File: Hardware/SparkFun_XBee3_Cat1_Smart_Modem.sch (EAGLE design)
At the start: 71 parts, among them J1 USB Female Type C Connector, J3 USB Female Type C Connector, J4 QWIIC_RIGHT_ANGLE, Q2 3.1A/30V/105mΩ, U1 FSUSB30MUX_MSOP10, U2 AP63203, U3 ESD Diode, U5 ESD Diode, U7 FT231XS

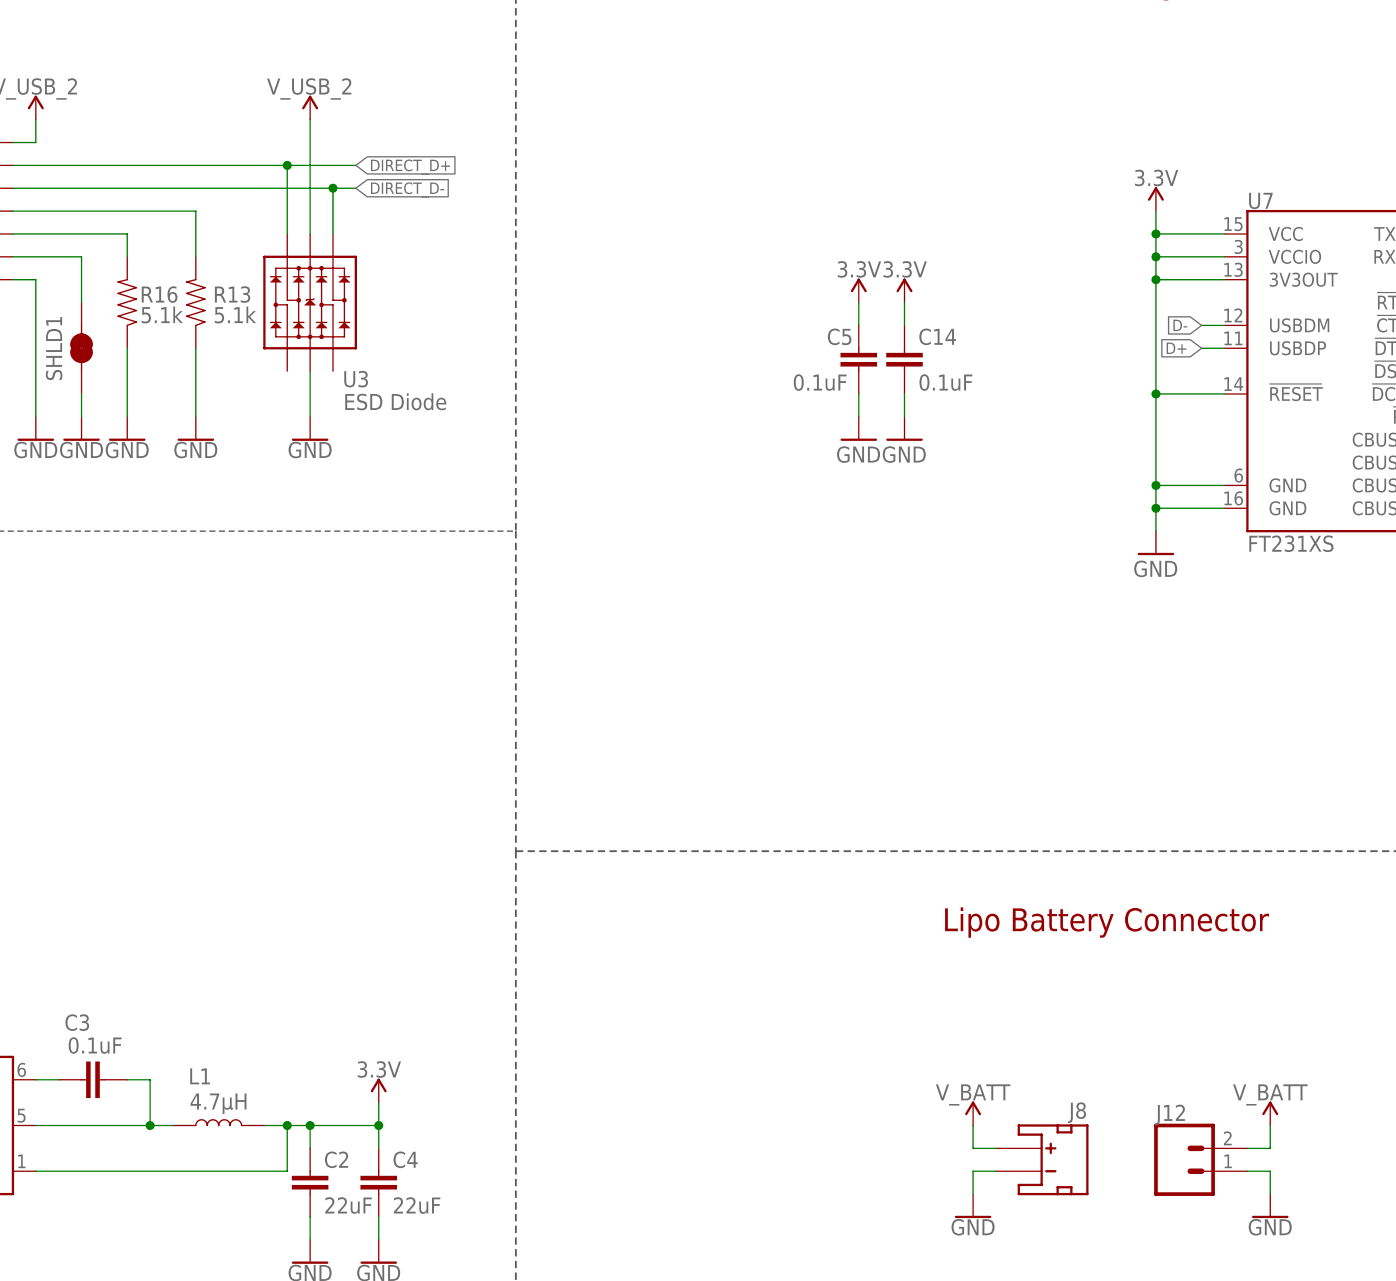
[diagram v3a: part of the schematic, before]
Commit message: Adds new 3.9uH Inductor
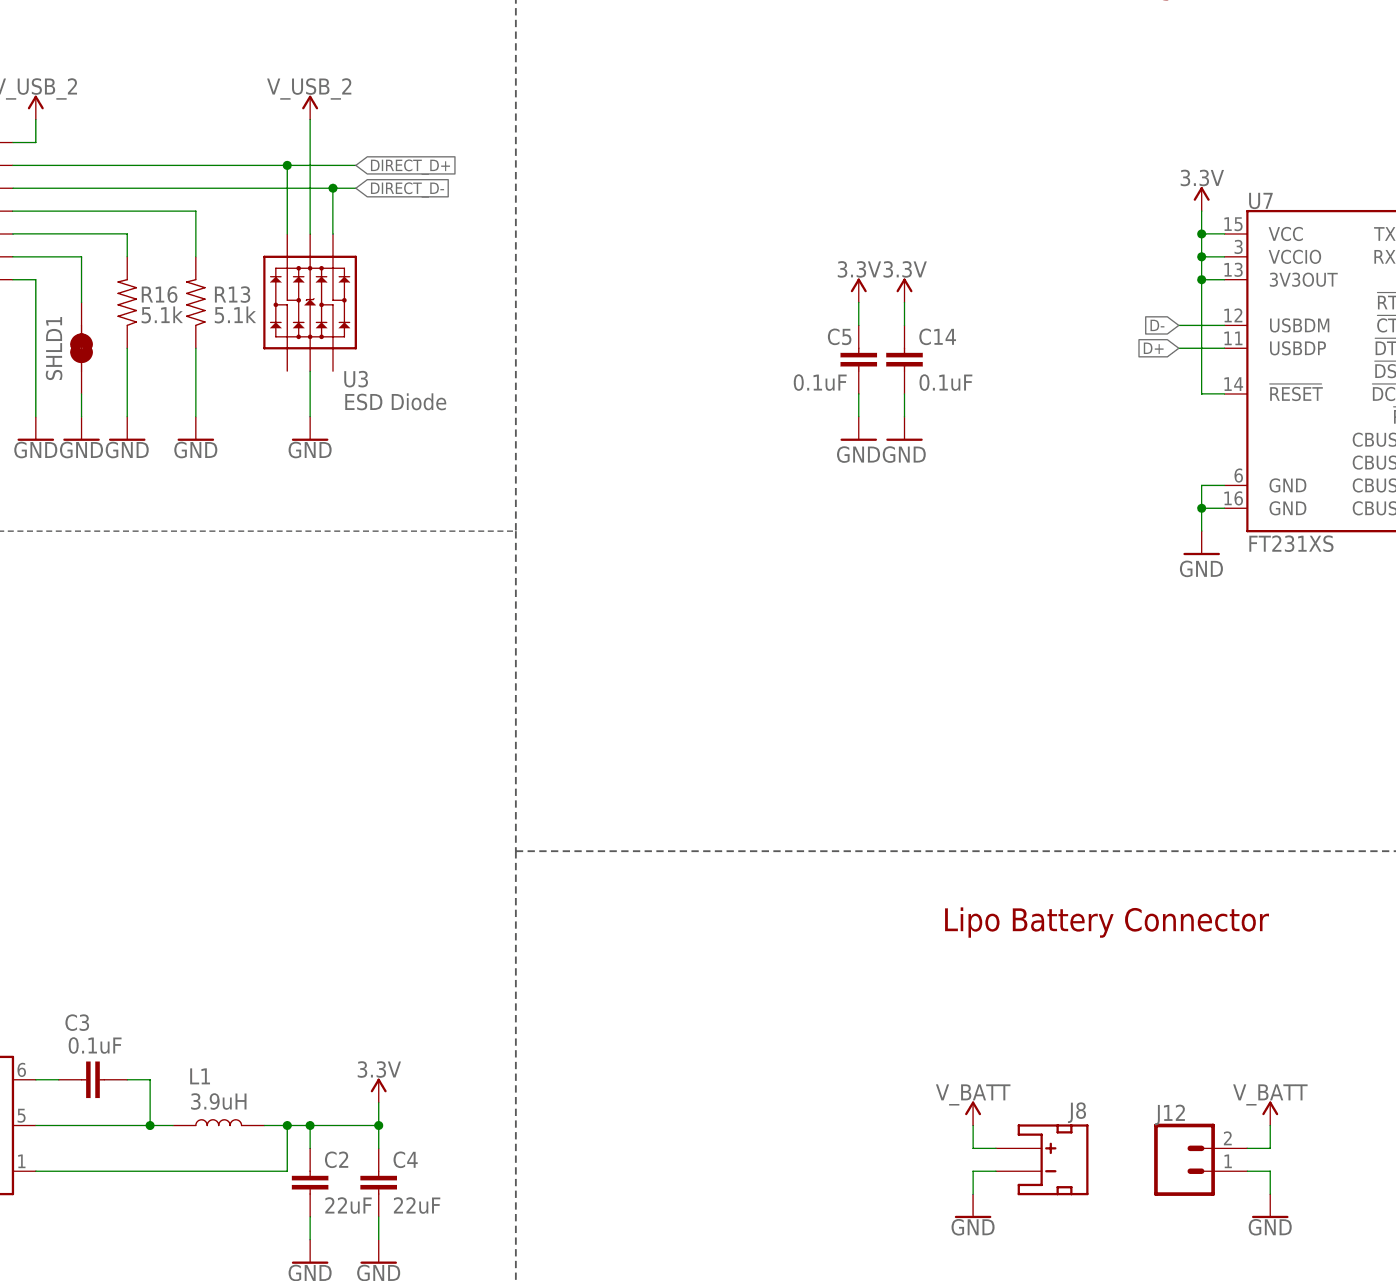
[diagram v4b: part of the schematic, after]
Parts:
- L1: value 4.7μH -> 3.9uH; device SparkFun-Coils:4.7μH_SHIELDED_INDUCTORNPIS_LS -> SparkFun-Coils:INDUCTOR-SRR4818A-3.9UH
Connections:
- net 3.3V: now also U7.!RESET, U7.3V3OUT, U7.VCC, U7.VCCIO
- net GND: no longer U7.!RESET, U7.3V3OUT, U7.VCC, U7.VCCIO
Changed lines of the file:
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@@
 <part name="LOGO3" library="SparkFun-Aesthetics" deviceset="QWIIC_LOGO" device="_5MM" value="QWIIC_LOGO_5MM"/>
 <part name="U2" library="SparkFun-IC-Power" deviceset="AP63203" device="" value="AP63203"/>
-<part name="L1" library="SparkFun-Coils" deviceset="4.7μH_SHIELDED_INDUCTOR" device="NPIS_LS" value="4.7μH"/>
+<part name="L1" library="SparkFun-Coils" deviceset="INDUCTOR" device="-SRR4818A-3.9UH" value="3.9uH"/>
 <part name="C3" library="SparkFun-Capacitors" deviceset="0.1UF" device="-0603-25V-5%" value="0.1uF"/>
 <part name="C2" library="SparkFun-Capacitors" deviceset="22UF" device="-0603-6.3V-20%" value="22uF"/>
@@
 <part name="GND37" library="SparkFun-PowerSymbols" deviceset="GND" device=""/>
 <part name="U7" library="SparkFun-IC-Comms" deviceset="FT231X" device="S" value="FT231XS"/>
-<part name="SUPPLY25" library="SparkFun-PowerSymbols" deviceset="3.3V" device=""/>
 <part name="GND39" library="SparkFun-PowerSymbols" deviceset="GND" device=""/>
 <part name="C14" library="SparkFun-Capacitors" deviceset="0.1UF" device="-0603-25V-(+80/-20%)" value="0.1uF"/>
@@
 <part name="SUPPLY21" library="SparkFun-PowerSymbols" deviceset="3.3V" device=""/>
 <part name="GND32" library="SparkFun-PowerSymbols" deviceset="GND" device=""/>
+<part name="SUPPLY22" library="SparkFun-PowerSymbols" deviceset="3.3V" device=""/>
 </parts>
 <sheets>
@@
 <attribute name="VALUE" x="223.52" y="132.08" size="1.778" layer="96" font="vector"/>
 </instance>
-<instance part="L1" gate="L1" x="261.62" y="142.24" smashed="yes" rot="R90">
+<instance part="L1" gate="G$1" x="261.62" y="142.24" smashed="yes" rot="R90">
 <attribute name="NAME" x="260.858" y="148.59" size="1.778" layer="95" font="vector" rot="R180"/>
 <attribute name="VALUE" x="264.922" y="144.018" size="1.778" layer="96" font="vector" rot="R180" align="top-left"/>
@@
 <attribute name="VALUE" x="375.92" y="207.772" size="1.778" layer="96" align="top-left"/>
 </instance>
-<instance part="SUPPLY25" gate="G$1" x="365.76" y="243.84" smashed="yes">
-<attribute name="VALUE" x="365.76" y="246.634" size="1.778" layer="96" font="vector" align="bottom-center"/>
-</instance>
-<instance part="GND39" gate="1" x="365.76" y="205.74" smashed="yes">
-<attribute name="VALUE" x="363.22" y="203.2" size="1.778" layer="96" font="vector"/>
+<instance part="GND39" gate="1" x="370.84" y="205.74" smashed="yes">
+<attribute name="VALUE" x="368.3" y="203.2" size="1.778" layer="96" font="vector"/>
 </instance>
 <instance part="C14" gate="G$1" x="337.82" y="226.06" smashed="yes">
@@
 <instance part="GND32" gate="1" x="337.82" y="218.44" smashed="yes">
 <attribute name="VALUE" x="335.28" y="215.9" size="1.778" layer="96" font="vector"/>
+</instance>
+<instance part="SUPPLY22" gate="G$1" x="370.84" y="243.84" smashed="yes">
+<attribute name="VALUE" x="370.84" y="246.634" size="1.778" layer="96" font="vector" align="bottom-center"/>
 </instance>
 </instances>
@@
 <segment>
 <pinref part="U7" gate="U$1" pin="GND@6"/>
+<wire x1="373.38" y1="213.36" x2="370.84" y2="213.36" width="0.1524" layer="91"/>
+<wire x1="370.84" y1="213.36" x2="370.84" y2="210.82" width="0.1524" layer="91"/>
 <pinref part="U7" gate="U$1" pin="GND@16"/>
-<wire x1="365.76" y1="213.36" x2="365.76" y2="210.82" width="0.1524" layer="91"/>
-<wire x1="365.76" y1="210.82" x2="365.76" y2="208.28" width="0.1524" layer="91"/>
+<wire x1="373.38" y1="210.82" x2="370.84" y2="210.82" width="0.1524" layer="91"/>
+<junction x="370.84" y="210.82"/>
+<wire x1="370.84" y1="210.82" x2="370.84" y2="208.28" width="0.1524" layer="91"/>
 <pinref part="GND39" gate="1" pin="GND"/>
-<wire x1="373.38" y1="210.82" x2="365.76" y2="210.82" width="0.1524" layer="91"/>
-<junction x="365.76" y="210.82"/>
-<wire x1="373.38" y1="213.36" x2="365.76" y2="213.36" width="0.1524" layer="91"/>
-<junction x="365.76" y="213.36"/>
-<pinref part="U7" gate="U$1" pin="VCCIO"/>
-<wire x1="373.38" y1="238.76" x2="365.76" y2="238.76" width="0.1524" layer="91"/>
-<wire x1="365.76" y1="238.76" x2="365.76" y2="241.3" width="0.1524" layer="91"/>
-<pinref part="U7" gate="U$1" pin="VCC"/>
-<wire x1="365.76" y1="241.3" x2="365.76" y2="243.84" width="0.1524" layer="91"/>
-<wire x1="373.38" y1="241.3" x2="365.76" y2="241.3" width="0.1524" layer="91"/>
-<junction x="365.76" y="241.3"/>
-<pinref part="SUPPLY25" gate="G$1" pin="3.3V"/>
-<junction x="365.76" y="238.76"/>
-<pinref part="U7" gate="U$1" pin="!RESET"/>
-<wire x1="365.76" y1="223.52" x2="365.76" y2="236.22" width="0.1524" layer="91"/>
-<wire x1="365.76" y1="236.22" x2="365.76" y2="238.76" width="0.1524" layer="91"/>
-<wire x1="373.38" y1="223.52" x2="365.76" y2="223.52" width="0.1524" layer="91"/>
-<pinref part="U7" gate="U$1" pin="3V3OUT"/>
-<wire x1="373.38" y1="236.22" x2="365.76" y2="236.22" width="0.1524" layer="91"/>
-<junction x="365.76" y="236.22"/>
-<wire x1="365.76" y1="213.36" x2="365.76" y2="223.52" width="0.1524" layer="91"/>
-<junction x="365.76" y="223.52"/>
 </segment>
 </net>
@@
 </segment>
 <segment>
-<pinref part="L1" gate="L1" pin="2"/>
+<pinref part="L1" gate="G$1" pin="2"/>
 <pinref part="C4" gate="G$1" pin="1"/>
 <wire x1="266.7" y1="142.24" x2="269.24" y2="142.24" width="0.1524" layer="91"/>
@@
 <wire x1="332.74" y1="231.14" x2="332.74" y2="233.68" width="0.1524" layer="91"/>
 </segment>
+<segment>
+<pinref part="U7" gate="U$1" pin="VCCIO"/>
+<wire x1="373.38" y1="238.76" x2="370.84" y2="238.76" width="0.1524" layer="91"/>
+<wire x1="370.84" y1="238.76" x2="370.84" y2="241.3" width="0.1524" layer="91"/>
+<pinref part="U7" gate="U$1" pin="VCC"/>
+<wire x1="370.84" y1="241.3" x2="370.84" y2="243.84" width="0.1524" layer="91"/>
+<wire x1="373.38" y1="241.3" x2="370.84" y2="241.3" width="0.1524" layer="91"/>
+<junction x="370.84" y="241.3"/>
+<junction x="370.84" y="238.76"/>
+<pinref part="U7" gate="U$1" pin="!RESET"/>
+<wire x1="370.84" y1="223.52" x2="370.84" y2="236.22" width="0.1524" layer="91"/>
+<wire x1="370.84" y1="236.22" x2="370.84" y2="238.76" width="0.1524" layer="91"/>
+<wire x1="373.38" y1="223.52" x2="370.84" y2="223.52" width="0.1524" layer="91"/>
+<pinref part="U7" gate="U$1" pin="3V3OUT"/>
+<wire x1="373.38" y1="236.22" x2="370.84" y2="236.22" width="0.1524" layer="91"/>
+<junction x="370.84" y="236.22"/>
+<pinref part="SUPPLY22" gate="G$1" pin="3.3V"/>
+</segment>
 </net>
 <net name="V_USB" class="0">
@@
 </segment>
 <segment>
-<wire x1="373.38" y1="228.6" x2="370.84" y2="228.6" width="0.1524" layer="91"/>
-<label x="370.84" y="228.6" size="1.27" layer="95" font="vector" rot="R180" xref="yes"/>
+<wire x1="373.38" y1="228.6" x2="368.3" y2="228.6" width="0.1524" layer="91"/>
+<label x="368.3" y="228.6" size="1.27" layer="95" font="vector" rot="R180" xref="yes"/>
 <pinref part="U7" gate="U$1" pin="USBDP"/>
 </segment>
@@
 </segment>
 <segment>
-<wire x1="373.38" y1="231.14" x2="370.84" y2="231.14" width="0.1524" layer="91"/>
-<label x="370.84" y="231.14" size="1.27" layer="95" font="vector" rot="R180" xref="yes"/>
+<wire x1="373.38" y1="231.14" x2="368.3" y2="231.14" width="0.1524" layer="91"/>
+<label x="368.3" y="231.14" size="1.27" layer="95" font="vector" rot="R180" xref="yes"/>
 <pinref part="U7" gate="U$1" pin="USBDM"/>
 </segment>
@@
 <segment>
 <pinref part="U2" gate="G$1" pin="SW"/>
-<pinref part="L1" gate="L1" pin="1"/>
+<pinref part="L1" gate="G$1" pin="1"/>
 <wire x1="241.3" y1="142.24" x2="254" y2="142.24" width="0.1524" layer="91"/>
 <pinref part="C3" gate="G$1" pin="2"/>

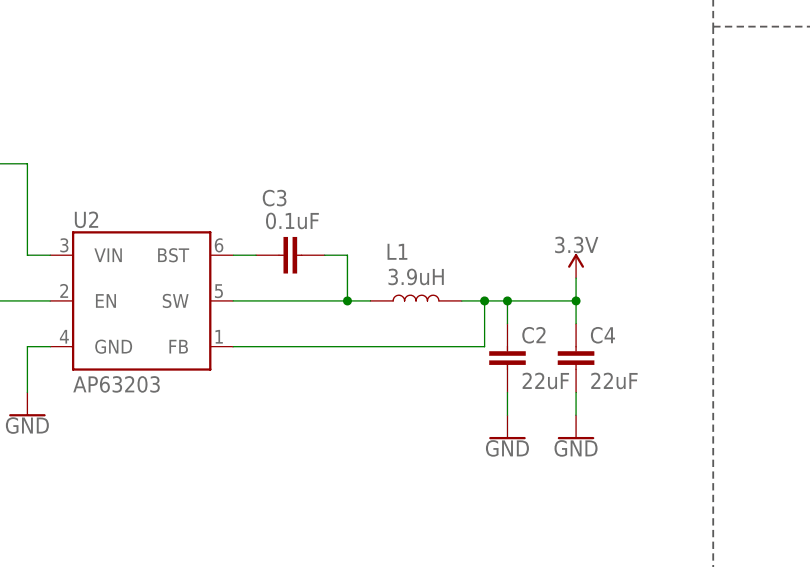
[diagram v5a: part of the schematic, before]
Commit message: Updates inductor to one with a higher saturation rating
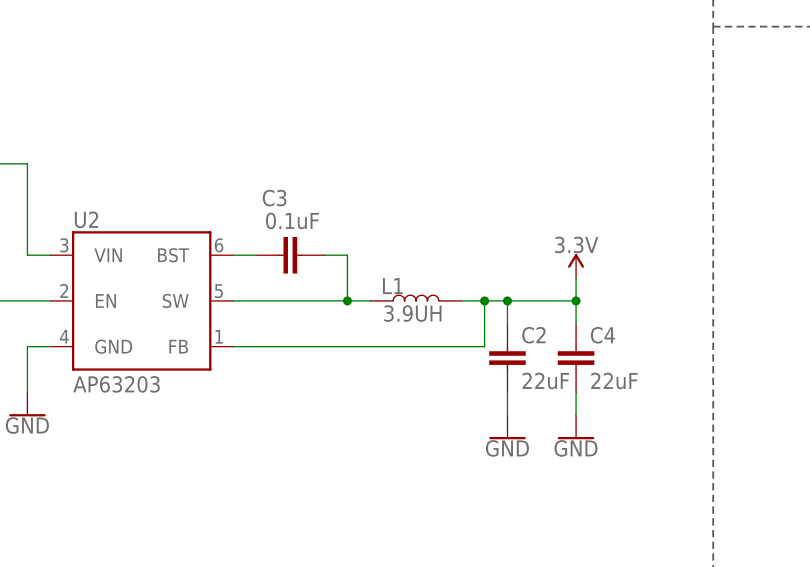
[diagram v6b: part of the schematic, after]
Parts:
- L1: value 3.9uH -> 3.9UH; device SparkFun-Coils:INDUCTOR-SRR4818A-3.9UH -> SparkFun-Coils:3.9UH
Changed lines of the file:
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@@
 <part name="LOGO3" library="SparkFun-Aesthetics" deviceset="QWIIC_LOGO" device="_5MM" value="QWIIC_LOGO_5MM"/>
 <part name="U2" library="SparkFun-IC-Power" deviceset="AP63203" device="" value="AP63203"/>
-<part name="L1" library="SparkFun-Coils" deviceset="INDUCTOR" device="-SRR4818A-3.9UH" value="3.9uH"/>
 <part name="C3" library="SparkFun-Capacitors" deviceset="0.1UF" device="-0603-25V-5%" value="0.1uF"/>
 <part name="C2" library="SparkFun-Capacitors" deviceset="22UF" device="-0603-6.3V-20%" value="22uF"/>
@@
 <part name="GND32" library="SparkFun-PowerSymbols" deviceset="GND" device=""/>
 <part name="SUPPLY22" library="SparkFun-PowerSymbols" deviceset="3.3V" device=""/>
+<part name="L1" library="SparkFun-Coils" deviceset="3.9UH" device=""/>
 </parts>
 <sheets>
@@
 <attribute name="VALUE" x="223.52" y="132.08" size="1.778" layer="96" font="vector"/>
 </instance>
-<instance part="L1" gate="G$1" x="261.62" y="142.24" smashed="yes" rot="R90">
-<attribute name="NAME" x="260.858" y="148.59" size="1.778" layer="95" font="vector" rot="R180"/>
-<attribute name="VALUE" x="264.922" y="144.018" size="1.778" layer="96" font="vector" rot="R180" align="top-left"/>
-</instance>
 <instance part="C3" gate="G$1" x="248.92" y="147.32" smashed="yes" rot="R90">
 <attribute name="NAME" x="247.396" y="154.559" size="1.778" layer="95" font="vector" rot="R180"/>
@@
 <instance part="SUPPLY22" gate="G$1" x="370.84" y="243.84" smashed="yes">
 <attribute name="VALUE" x="370.84" y="246.634" size="1.778" layer="96" font="vector" align="bottom-center"/>
+</instance>
+<instance part="L1" gate="G$1" x="261.62" y="142.24" smashed="yes" rot="R90">
+<attribute name="NAME" x="260.35" y="144.78" size="1.778" layer="95" font="vector" rot="R180"/>
+<attribute name="VALUE" x="264.668" y="139.954" size="1.778" layer="96" font="vector" rot="R180" align="top-left"/>
 </instance>
 </instances>
@@
 </segment>
 <segment>
-<pinref part="L1" gate="G$1" pin="2"/>
 <pinref part="C4" gate="G$1" pin="1"/>
 <wire x1="266.7" y1="142.24" x2="269.24" y2="142.24" width="0.1524" layer="91"/>
@@
 <wire x1="279.4" y1="144.78" x2="279.4" y2="142.24" width="0.1524" layer="91"/>
 <junction x="279.4" y="142.24"/>
+<pinref part="L1" gate="G$1" pin="2"/>
 </segment>
 <segment>
@@
 <segment>
 <pinref part="U2" gate="G$1" pin="SW"/>
-<pinref part="L1" gate="G$1" pin="1"/>
 <wire x1="241.3" y1="142.24" x2="254" y2="142.24" width="0.1524" layer="91"/>
 <pinref part="C3" gate="G$1" pin="2"/>
@@
 <wire x1="254" y1="147.32" x2="254" y2="142.24" width="0.1524" layer="91"/>
 <junction x="254" y="142.24"/>
-</segment>
-</net>
+<pinref part="L1" gate="G$1" pin="1"/>
+</segment>
+</net>
